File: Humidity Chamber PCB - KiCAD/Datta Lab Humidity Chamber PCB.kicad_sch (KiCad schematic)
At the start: 23 parts, among them J1 BNC-1, J2 BNC-2, J3 Cam-1, J4 Cam-2, J5 Cam-3, J6 GPIO Breakout Header, J7 +24 VDC, J8 A00-432-262-450, SW1 500SSP1S1M6QEA, U1 Teensy4.1

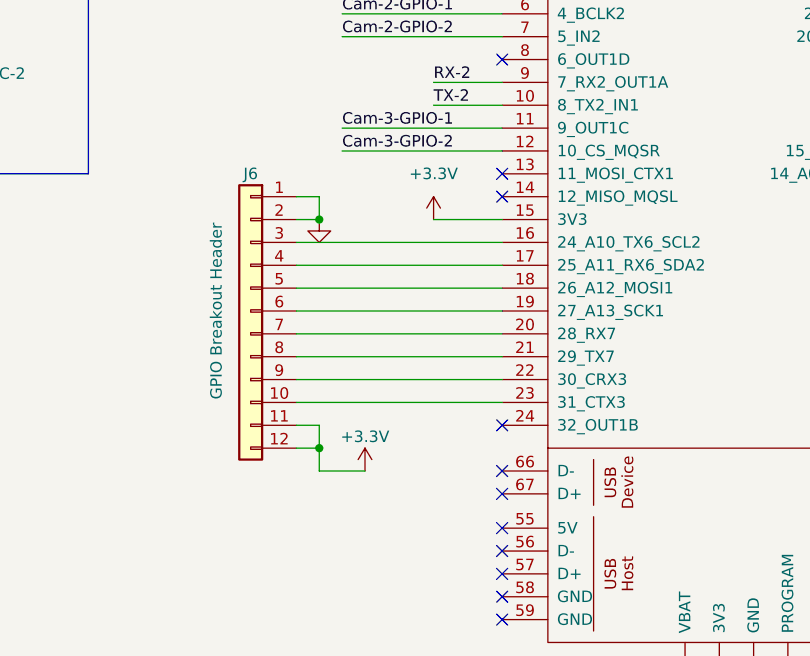
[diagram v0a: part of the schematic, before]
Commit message: Routed all traces
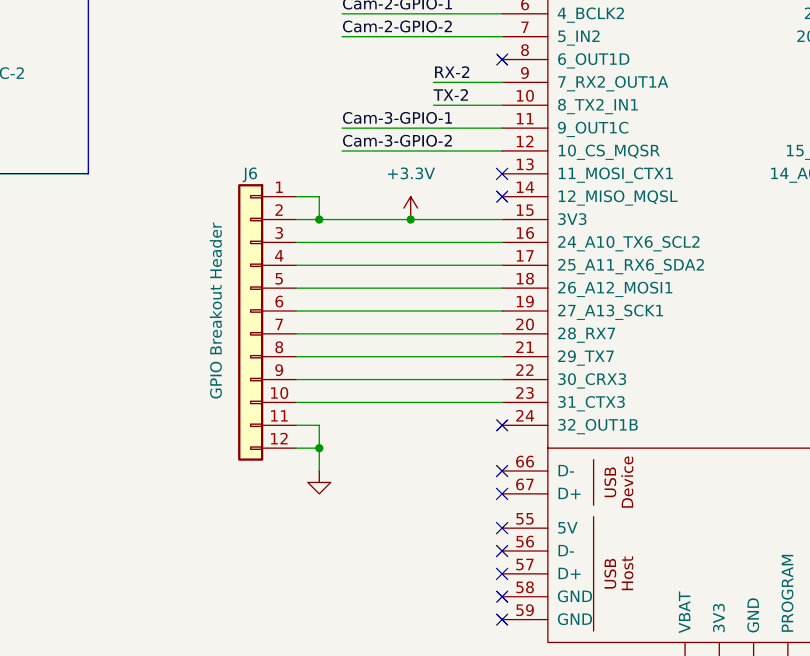
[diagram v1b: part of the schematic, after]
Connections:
- net +3.3V: now also J6.1 (Pin_1), J6.2 (Pin_2); no longer J6.11 (Pin_11), J6.12 (Pin_12)
- net GND: now also J6.11 (Pin_11), J6.12 (Pin_12); no longer J6.1 (Pin_1), J6.2 (Pin_2)
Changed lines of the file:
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@@
 	)
 	(junction
-		(at 160.02 33.02)
+		(at 73.66 63.5)
 		(diameter 0)
 		(color 0 0 0 0)
 	)
 	(junction
-		(at 165.1 33.02)
+		(at 160.02 33.02)
 		(diameter 0)
 		(color 0 0 0 0)
 	)
 	(junction
-		(at 73.66 63.5)
+		(at 165.1 33.02)
 		(diameter 0)
 		(color 0 0 0 0)
@@
 	)
 	(junction
+		(at 83.82 63.5)
+		(diameter 0)
+		(color 0 0 0 0)
+	)
+	(junction
 		(at 132.08 137.16)
 		(diameter 0)
@@
 	(wire
 		(pts
+			(xy 73.66 63.5) (xy 83.82 63.5)
+		)
+		(stroke
+			(width 0)
+			(type default)
+		)
+	)
+	(wire
+		(pts
 			(xy 73.66 91.44) (xy 73.66 88.9)
 		)
@@
 	(wire
 		(pts
+			(xy 83.82 63.5) (xy 93.98 63.5)
+		)
+		(stroke
+			(width 0)
+			(type default)
+		)
+	)
+	(wire
+		(pts
 			(xy 195.58 157.48) (xy 203.2 157.48)
 		)
@@
 	(wire
 		(pts
-			(xy 78.74 91.44) (xy 73.66 91.44)
-		)
-		(stroke
-			(width 0)
-			(type default)
-		)
-	)
-	(wire
-		(pts
 			(xy 30.48 154.94) (xy 48.26 154.94)
 		)
@@
 	(wire
 		(pts
-			(xy 93.98 63.5) (xy 86.36 63.5)
-		)
-		(stroke
-			(width 0)
-			(type default)
-		)
-	)
-	(wire
-		(pts
 			(xy 45.72 157.48) (xy 48.26 157.48)
 		)
@@
 	)
 	(symbol
-		(lib_id "power:+3.3V")
-		(at 78.74 91.44 0)
-		(unit 1)
-		(exclude_from_sim no)
-		(in_bom yes)
-		(on_board yes)
-		(dnp no)
-		(property "Reference" "#PWR07"
-			(at 78.74 95.25 0)
-			(effects
-				(font
-					(size 1.27 1.27)
-				)
-				(hide yes)
-			)
-		)
-		(property "Value" "+3.3V"
-			(at 78.74 87.63 0)
-			(effects
-				(font
-					(size 1.27 1.27)
-				)
-			)
-		)
-		(property "Footprint" ""
-			(at 78.74 91.44 0)
-			(effects
-				(font
-					(size 1.27 1.27)
-				)
-				(hide yes)
-			)
-		)
-		(property "Datasheet" ""
-			(at 78.74 91.44 0)
-			(effects
-				(font
-					(size 1.27 1.27)
-				)
-				(hide yes)
-			)
-		)
-		(property "Description" "Power symbol creates a global label with name \"+3.3V\""
-			(at 78.74 91.44 0)
-			(effects
-				(font
-					(size 1.27 1.27)
-				)
-				(hide yes)
-			)
-		)
-		(pin "1"
-		)
-		(instances
-			(project "HMS Olfactometer"
-				(path "/d7d8f86e-c8d6-438e-95be-a4e29dfe527f"
-					(reference "#PWR07")
-					(unit 1)
-				)
-			)
-		)
-	)
-	(symbol
 		(lib_id "Switch:SW_SPST")
 		(at 124.46 137.16 0)
@@
 	(symbol
 		(lib_id "power:GND")
-		(at 73.66 63.5 0)
+		(at 73.66 91.44 0)
 		(unit 1)
 		(exclude_from_sim no)
@@
 		(fields_autoplaced yes)
 		(property "Reference" "#PWR06"
-			(at 73.66 69.85 0)
+			(at 73.66 97.79 0)
 			(effects
 				(font
@@
 		)
 		(property "Value" "GND"
-			(at 73.66 68.58 0)
+			(at 73.66 96.52 0)
 			(effects
 				(font
@@
 		)
 		(property "Footprint" ""
-			(at 73.66 63.5 0)
+			(at 73.66 91.44 0)
 			(effects
 				(font
@@
 		)
 		(property "Datasheet" ""
-			(at 73.66 63.5 0)
+			(at 73.66 91.44 0)
 			(effects
 				(font
@@
 		)
 		(property "Description" "Power symbol creates a global label with name \"GND\" , ground"
-			(at 73.66 63.5 0)
+			(at 73.66 91.44 0)
 			(effects
 				(font
@@
 		)
 		(instances
-			(project "HMS Olfactometer"
+			(project "Datta Lab Humidity Chamber PCB"
 				(path "/d7d8f86e-c8d6-438e-95be-a4e29dfe527f"
 					(reference "#PWR06")
@@
 	(symbol
 		(lib_id "power:+3.3V")
-		(at 86.36 63.5 0)
+		(at 83.82 63.5 0)
 		(mirror y)
 		(unit 1)
@@
 		(dnp no)
 		(property "Reference" "#PWR08"
-			(at 86.36 67.31 0)
+			(at 83.82 67.31 0)
 			(effects
 				(font
@@
 		)
 		(property "Value" "+3.3V"
-			(at 86.36 58.42 0)
+			(at 83.82 58.42 0)
 			(effects
 				(font
@@
 		)
 		(property "Footprint" ""
-			(at 86.36 63.5 0)
+			(at 83.82 63.5 0)
 			(effects
 				(font
@@
 		)
 		(property "Datasheet" ""
-			(at 86.36 63.5 0)
+			(at 83.82 63.5 0)
 			(effects
 				(font
@@
 		)
 		(property "Description" "Power symbol creates a global label with name \"+3.3V\""
-			(at 86.36 63.5 0)
+			(at 83.82 63.5 0)
 			(effects
 				(font

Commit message: Minor cosmetic adjustments
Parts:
- removed H3, H4: MountingHole, MountingHole:MountingHole_3.2mm_M3, symbol Mechanical:MountingHole
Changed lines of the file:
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@@
-	)
-	(symbol
-		(lib_id "Mechanical:MountingHole")
-		(at 106.68 195.58 0)
-		(unit 1)
-		(exclude_from_sim yes)
-		(in_bom no)
-		(on_board yes)
-		(dnp no)
-		(fields_autoplaced yes)
-		(property "Reference" "H4"
-			(at 109.22 194.3099 0)
-			(effects
-				(font
-					(size 1.27 1.27)
-				)
-				(justify left)
-			)
-		)
-		(property "Value" "MountingHole"
-			(at 109.22 196.8499 0)
-			(effects
-				(font
-					(size 1.27 1.27)
-				)
-				(justify left)
-				(hide yes)
-			)
-		)
-		(property "Footprint" "MountingHole:MountingHole_3.2mm_M3"
-			(at 106.68 195.58 0)
-			(effects
-				(font
-					(size 1.27 1.27)
-				)
-				(hide yes)
-			)
-		)
-		(property "Datasheet" "~"
-			(at 106.68 195.58 0)
-			(effects
-				(font
-					(size 1.27 1.27)
-				)
-				(hide yes)
-			)
-		)
-		(property "Description" "Mounting Hole without connection"
-			(at 106.68 195.58 0)
-			(effects
-				(font
-					(size 1.27 1.27)
-				)
-				(hide yes)
-			)
-		)
-		(instances
-			(project ""
-				(path "/d7d8f86e-c8d6-438e-95be-a4e29dfe527f"
-					(reference "H4")
-					(unit 1)
-				)
-			)
-		)
 	)
 	(symbol
@@
 					(unit 1)
 				)
-			)
-		)
-	)
-	(symbol
-		(lib_id "Mechanical:MountingHole")
-		(at 106.68 190.5 0)
-		(unit 1)
-		(exclude_from_sim yes)
-		(in_bom no)
-		(on_board yes)
-		(dnp no)
-		(fields_autoplaced yes)
-		(property "Reference" "H3"
-			(at 109.22 189.2299 0)
-			(effects
-				(font
-					(size 1.27 1.27)
-				)
-				(justify left)
-			)
-		)
-		(property "Value" "MountingHole"
-			(at 109.22 191.7699 0)
-			(effects
-				(font
-					(size 1.27 1.27)
-				)
-				(justify left)
-				(hide yes)
-			)
-		)
-		(property "Footprint" "MountingHole:MountingHole_3.2mm_M3"
-			(at 106.68 190.5 0)
-			(effects
-				(font
-					(size 1.27 1.27)
-				)
-				(hide yes)
-			)
-		)
-		(property "Datasheet" "~"
-			(at 106.68 190.5 0)
-			(effects
-				(font
-					(size 1.27 1.27)
-				)
-				(hide yes)
-			)
-		)
-		(property "Description" "Mounting Hole without connection"
-			(at 106.68 190.5 0)
-			(effects
-				(font
-					(size 1.27 1.27)
-				)
-				(hide yes)
-			)
-		)
-		(instances
-			(project ""
-				(path "/d7d8f86e-c8d6-438e-95be-a4e29dfe527f"
-					(reference "H3")
-					(unit 1)
-				)
